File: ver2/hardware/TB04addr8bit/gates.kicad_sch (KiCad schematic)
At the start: 16 parts, among them U1501 74AHC04, U1502 74AHC04, U1503 74LS08, U1504 74HC00, U1505 74LS00, U1506 74LS32, U1507 74LS08, U1508 74HC00

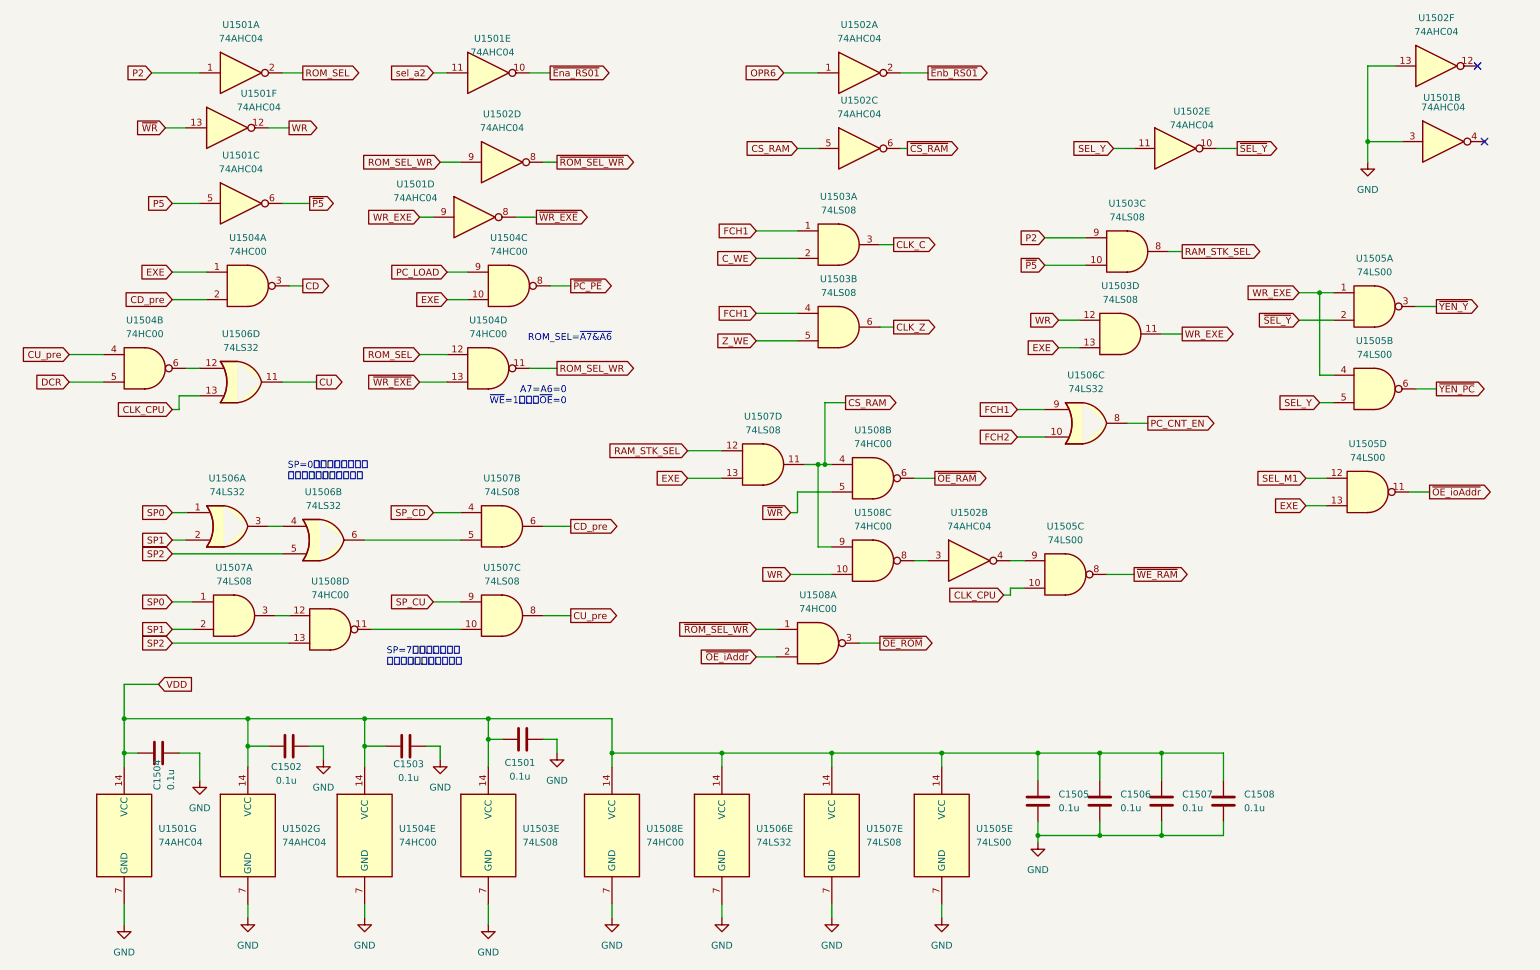
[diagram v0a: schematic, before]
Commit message: ver2: 論理ゲートを整理(9→8パッケージ・38→31ゲート)
・~OE_ROMをU1504から直結し、ROM_SEL_WR/~ROM_SEL_WRの対を廃止
  (冗長なOE_iAddr項を除去。これが唯一の論理変更)
・WRと~SEL_YをROM-Cの予備bitから出しインバータ2個を削減
・~WE_RAMとSP_NE7をU1509(74LS10)の3入力NANDに集約
・SP_NE0/CU_rawのラベルを追加し無名ネットを解消
・U1502/U1508/C1508を削除、U1509を追加
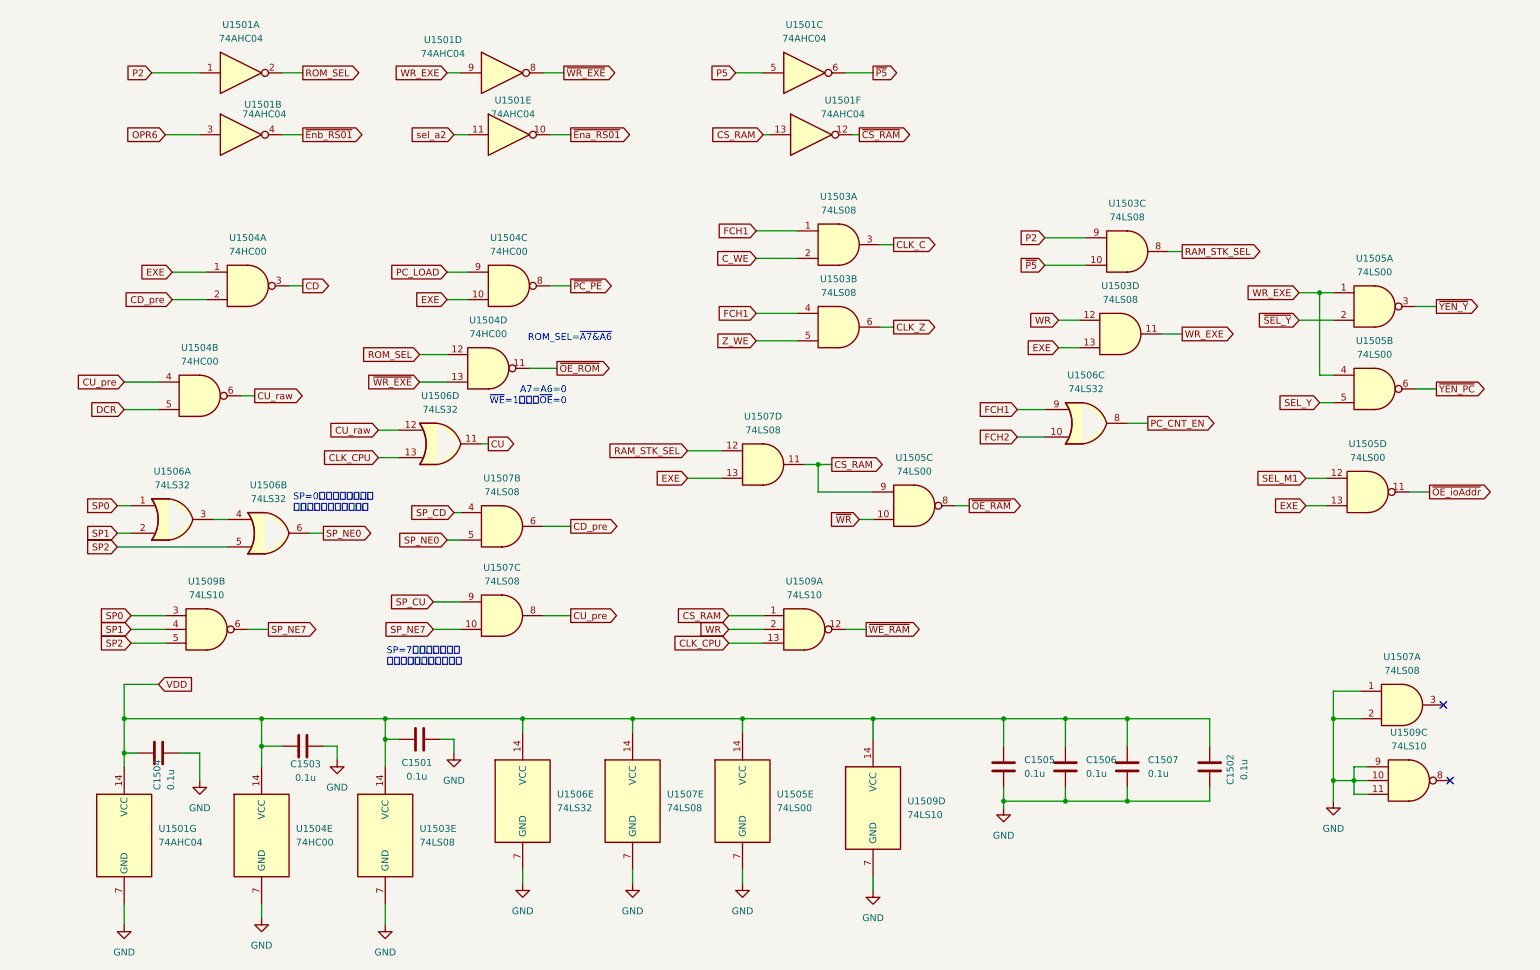
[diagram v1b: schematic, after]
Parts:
- removed C1508: 0.1u, symbol Device:C
- removed U1502: 74AHC04, symbol 74xx:74AHC04
- removed U1508: 74HC00, symbol 74xx:74HC00
- added U1509: 74LS10, symbol 74xx:74LS10
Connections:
- net ROM_SEL_WR is gone; now on net ~{OE_ROM}: U1504.11
- net CLK_CPU: now also U1509.13; no longer U1505.10
- net CS_RAM: now also U1501.13, U1505.9, U1509.1
- net GND: now also C1502.1, U1507.1, U1507.2, U1509.10, U1509.11, U1509.7 (GND), U1509.9; no longer C1502.2, U1501.3
- net OPR6: now also U1501.3
- net SP0: now also U1509.3; no longer U1507.1
- net SP1: now also U1509.4; no longer U1507.2
- net SP2: now also U1509.5
- net VDD: now also C1502.2, U1509.14 (VCC); no longer C1502.1
- net WR: now also U1509.2; no longer U1501.12
- net ~{CS_RAM}: now also U1501.12
- net ~{Enb_RS01}: now also U1501.4
- net ~{OE_RAM}: now also U1505.8
- net ~{WE_RAM}: now also U1509.12; no longer U1505.8
- net ~{WR}: now also U1505.10; no longer U1501.13
- net SP_NE7: now reaches U1507.10
- net SP_NE7: now also U1509.6
- net CU_raw: now reaches U1504.6, U1506.12
- net SP_NE0: now reaches U1506.6, U1507.5
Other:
- moved on the sheet: C1501, C1502, C1503, C1505, C1506, C1507, U1501B, U1501C, U1501D, U1501E, U1501F, U1503E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
